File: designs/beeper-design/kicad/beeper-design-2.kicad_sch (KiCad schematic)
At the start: 26 parts, among them U14 EVPBB4A9B000, U15 EVPBB4A9B000, U16 EVPBB4A9B000, U4 DA7212-01UM2, U9 LSM6DSOXTR

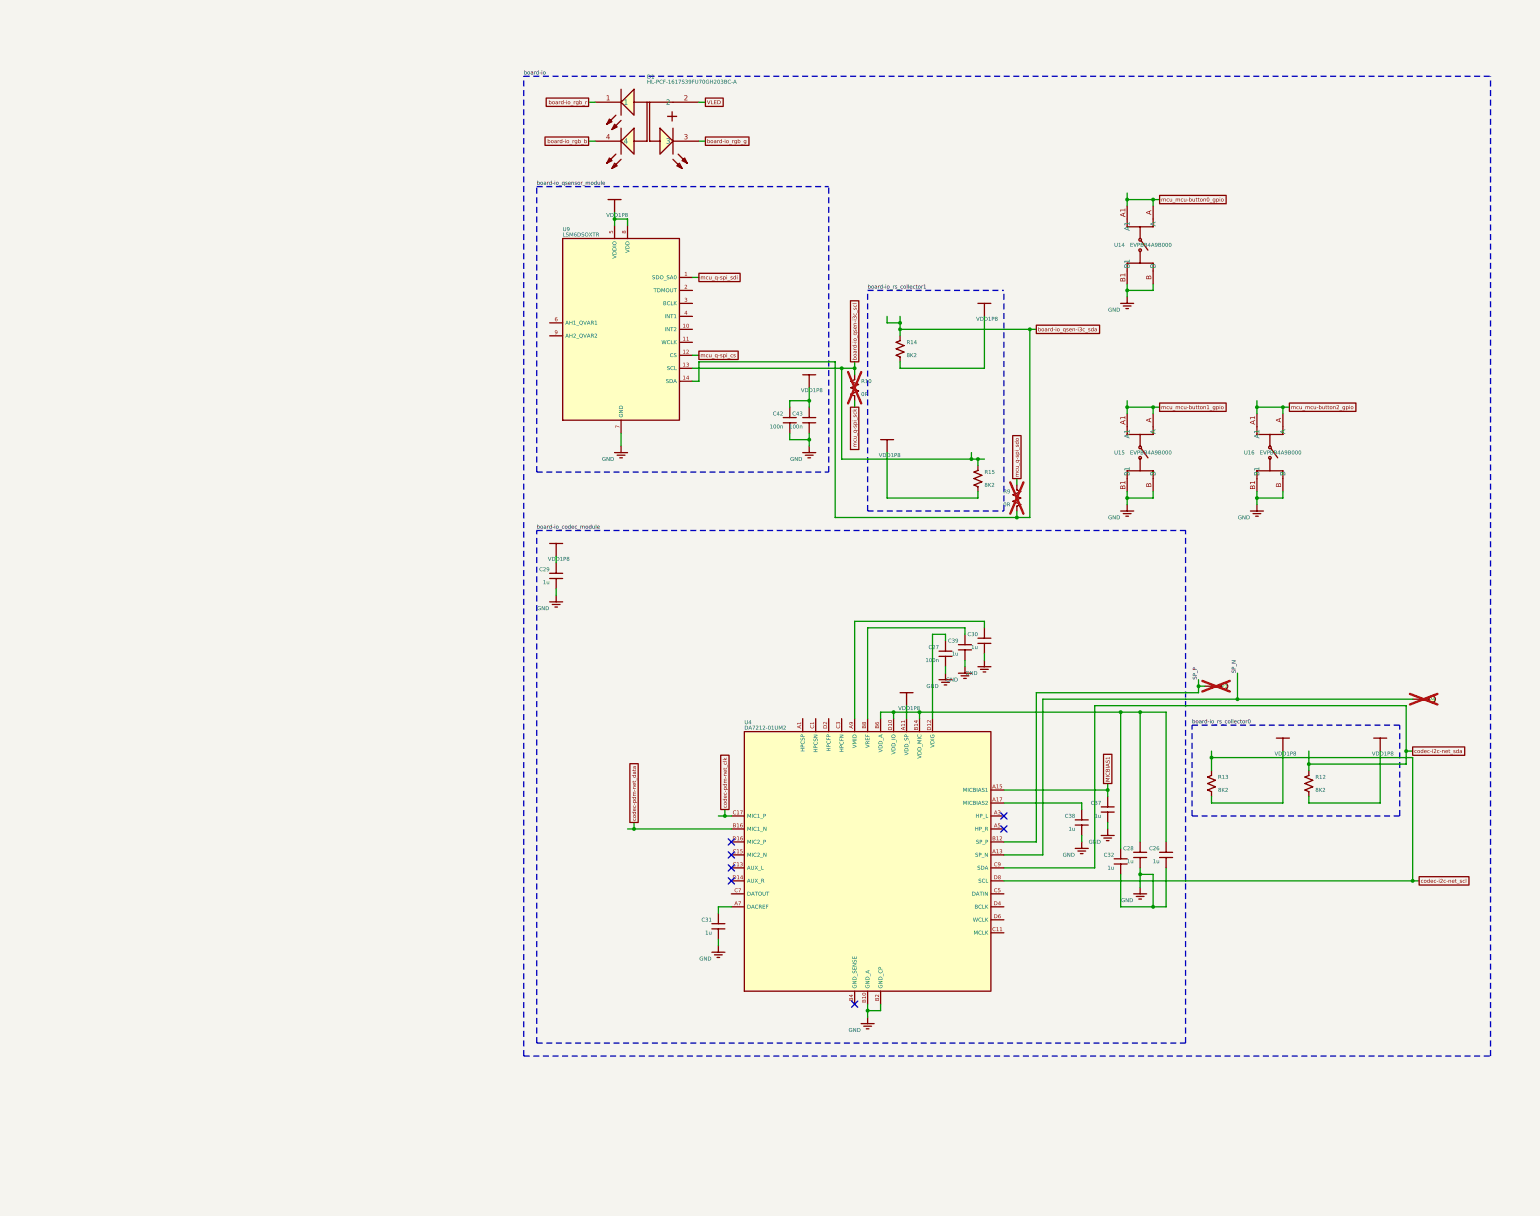
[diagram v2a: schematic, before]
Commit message: fixing drc errors
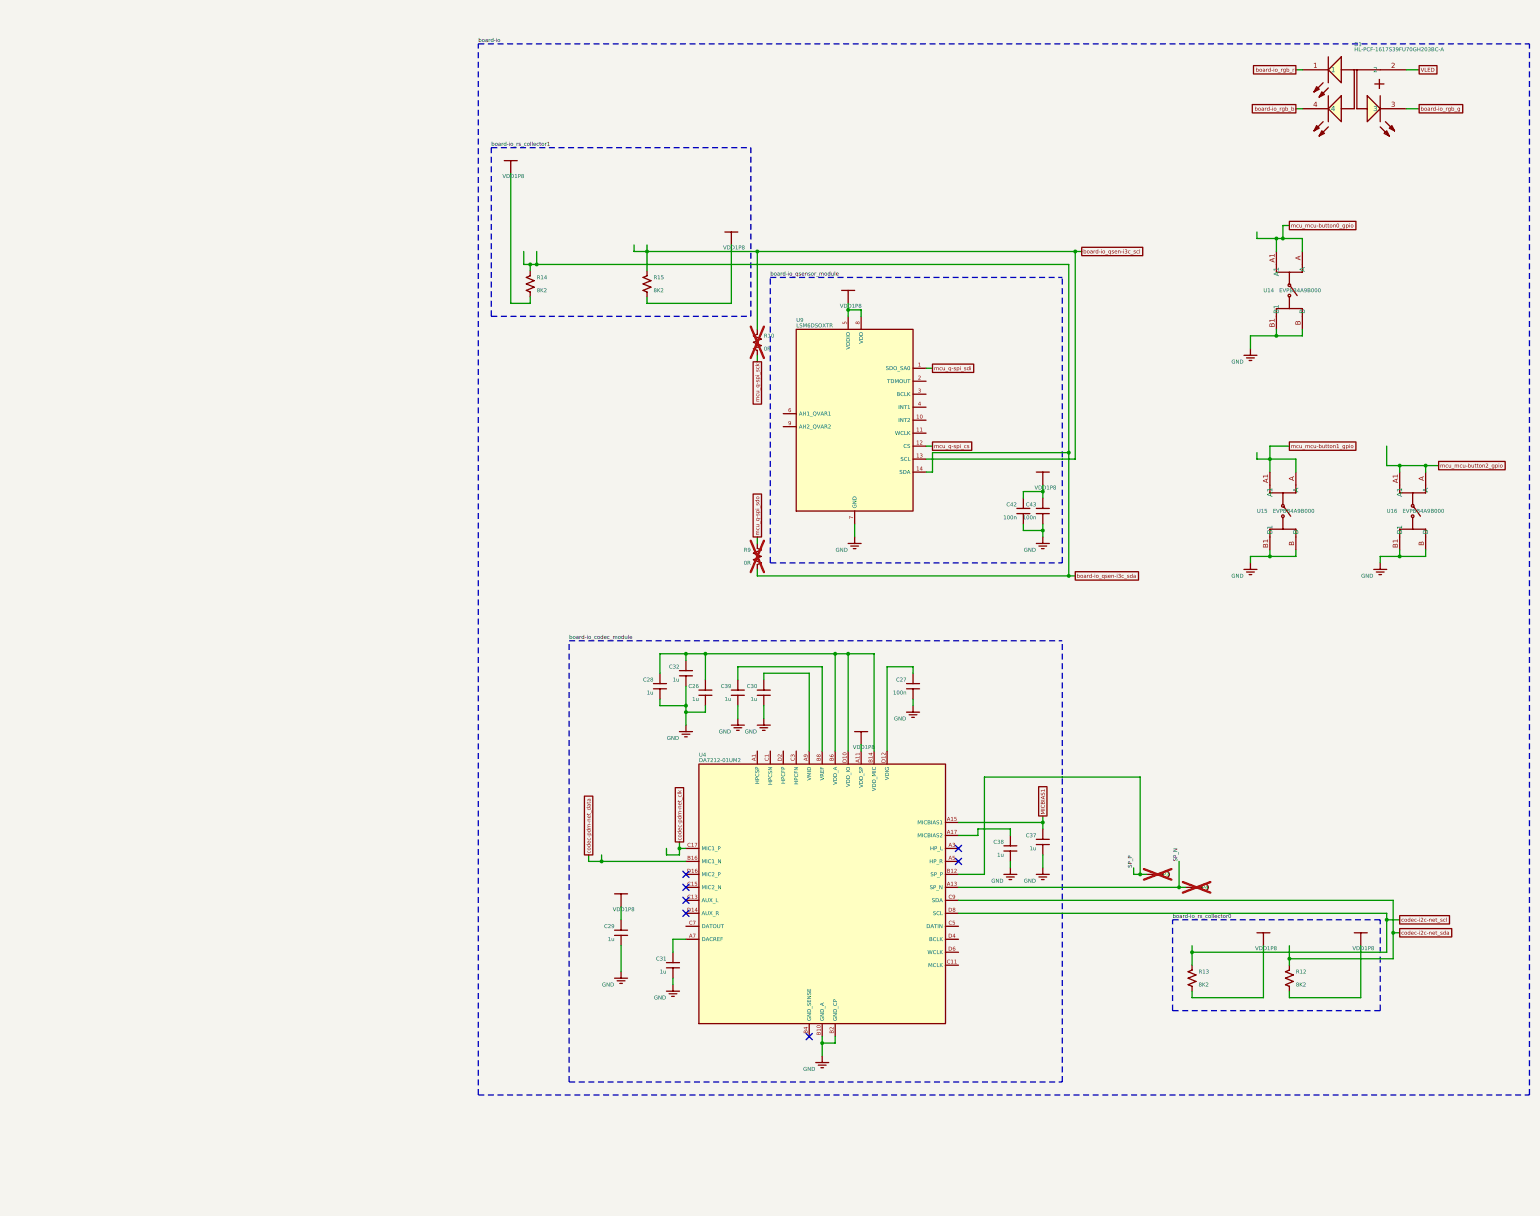
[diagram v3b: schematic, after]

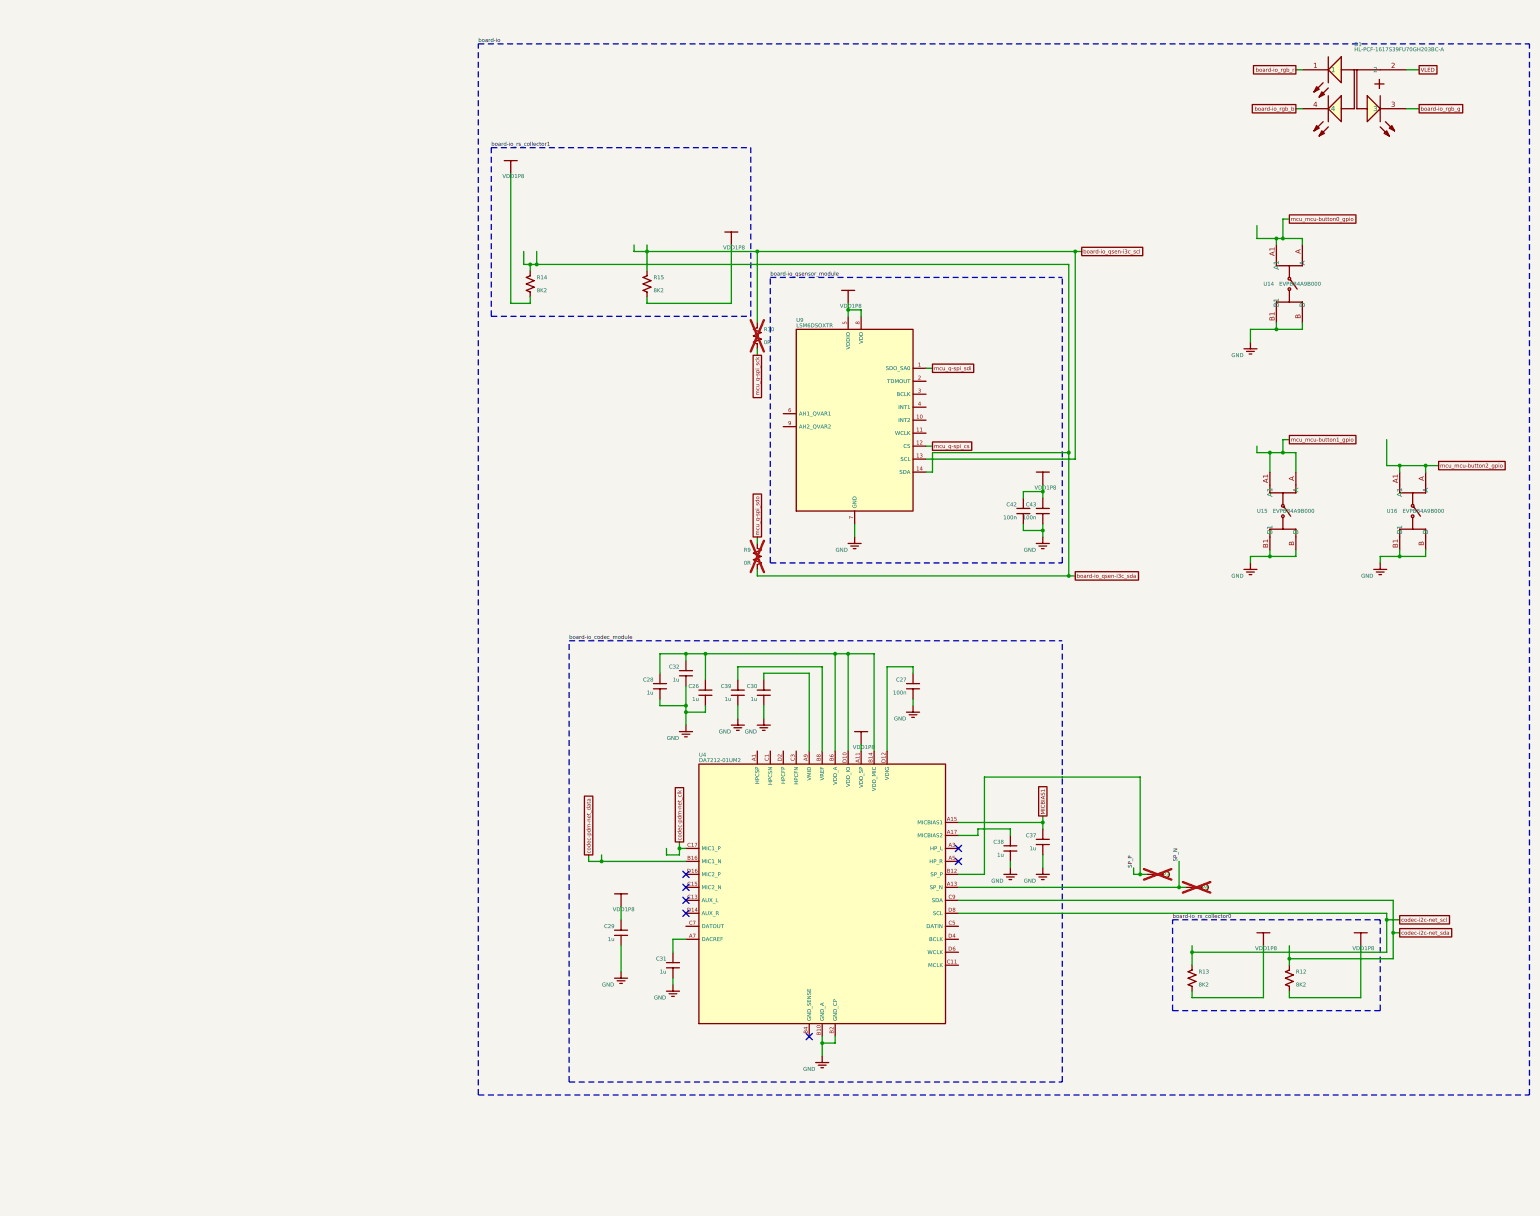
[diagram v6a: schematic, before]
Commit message: made ocdb a submodule
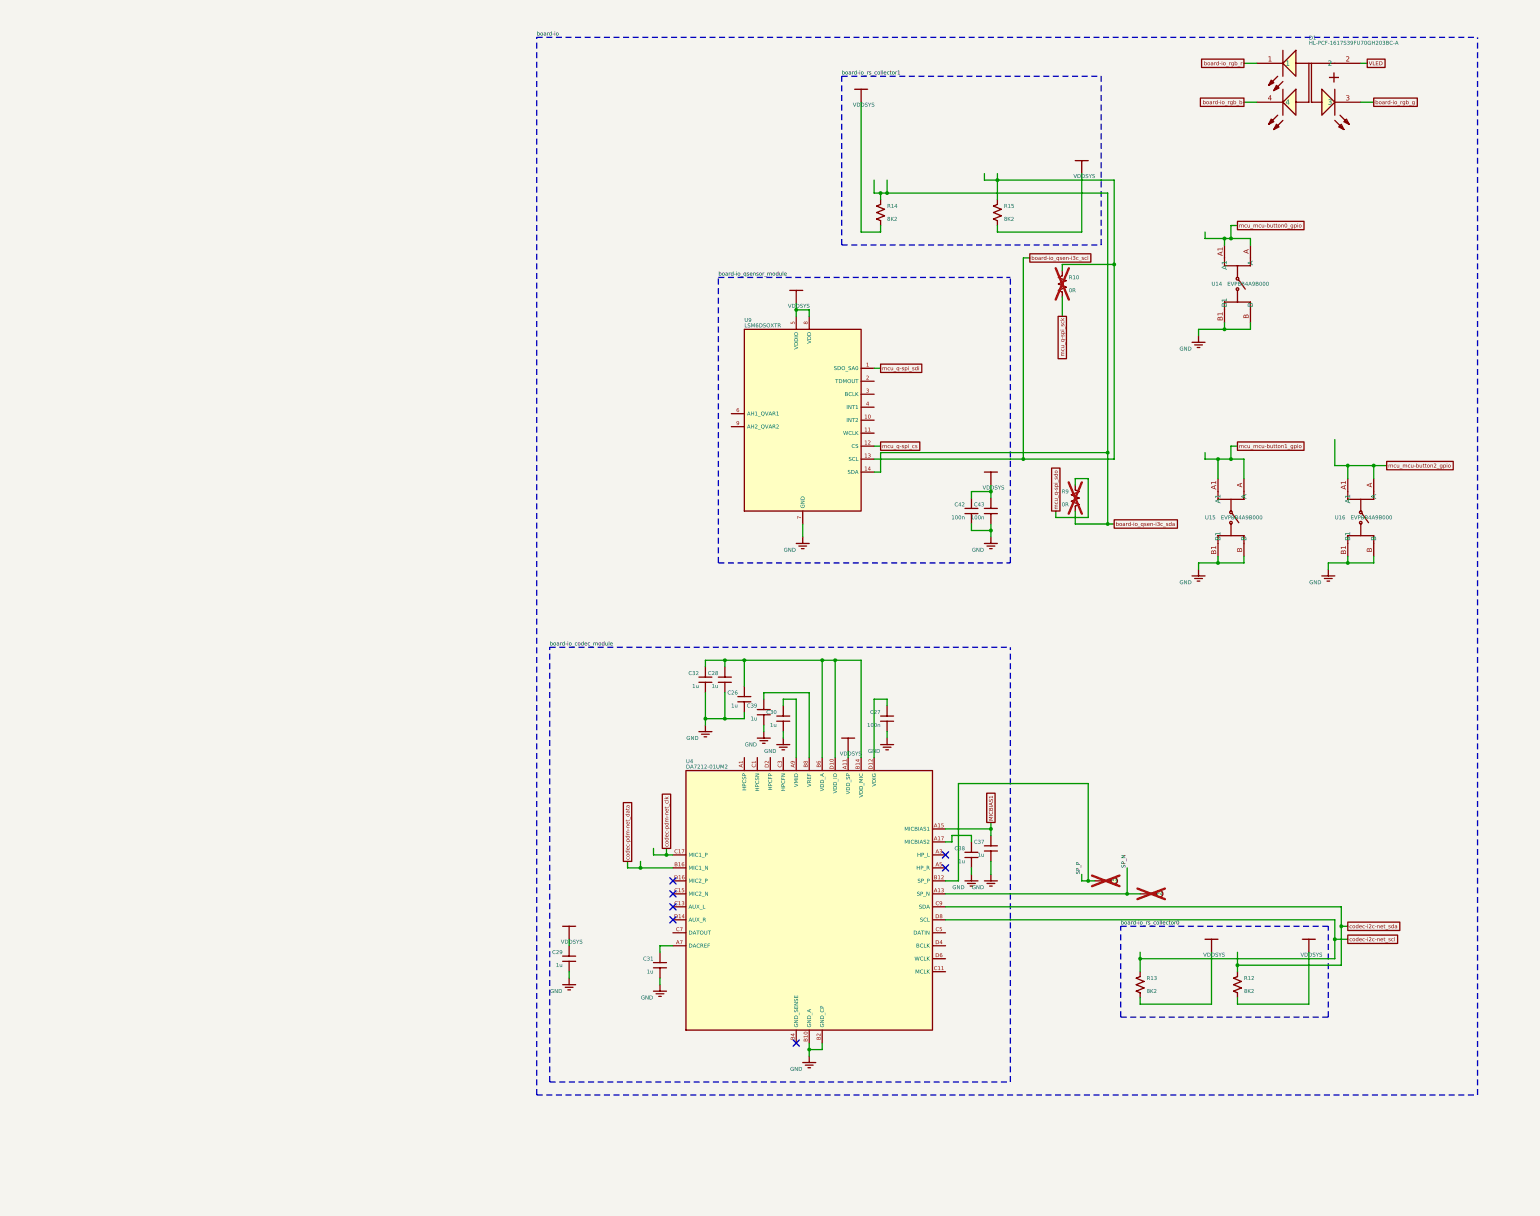
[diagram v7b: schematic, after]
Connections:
- net VDD1P8 renamed VDDSYS

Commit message: kicad exported data
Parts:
- removed C26: 1u, beeper-design:Pkg0201_27, symbol C76935_8
- removed C27: 100n, beeper-design:Pkg0201_38, symbol my_capacitor_13
- removed C28: 1u, beeper-design:Pkg0201_5, symbol C76935_1
- removed C29: 1u, beeper-design:Pkg0201_15, symbol C76935_5
- removed C30: 1u, beeper-design:Pkg0201_3, symbol C76935
- removed C31: 1u, beeper-design:Pkg0201_13, symbol C76935_4
- removed C32: 1u, beeper-design:Pkg0201_23, symbol C76935_6
- removed C37: 1u, beeper-design:Pkg0201_26, symbol C76935_7
- removed C38: 1u, beeper-design:Pkg0201_37, symbol C76935_10
- removed C39: 1u, beeper-design:Pkg0201_35, symbol C76935_9
- removed C42: 100n, beeper-design:Pkg0201_29, symbol my_capacitor_8
- removed C43: 100n, beeper-design:Pkg0201_39, symbol my_capacitor_14
- removed R10: 0R, beeper-design:Pkg0201_28, symbol my_resistor_8
- removed R12, R13: 8K2, beeper-design:Pkg0201_17, symbol my_resistor_4
- removed R14, R15: 8K2, beeper-design:Pkg0201_1, symbol my_resistor
- removed R9: 0R, beeper-design:Pkg0201_19, symbol my_resistor_5
- removed U4: DA7212-01UM2, beeper-design:LP_3, symbol component_1
- added C26: 2.2u, beeper-design:Pkg0201_19, symbol C335106_10
- added C27: 2.2u, beeper-design:Pkg0201_33, symbol C335106_21
- added C28: 2.2u, beeper-design:Pkg0201_46, symbol C335106_28
- added C29: 2.2u, beeper-design:Pkg0201_3, symbol C335106
- added C30: 2.2u, beeper-design:Pkg0201_43, symbol C335106_27
- added C31: 2.2u, beeper-design:Pkg0201, symbol C335106_36
- added C32: 2.2u, beeper-design:Pkg0201_12, symbol C335106_6
- added C37: 2.2u, beeper-design:Pkg0201_17, symbol C335106_8
- added C38: 2.2u, beeper-design:Pkg0201_31, symbol C335106_20
- added C39: 2.2u, beeper-design:Pkg0201_28, symbol C335106_18
- added C42: 2.2u, beeper-design:Pkg0201_21, symbol C335106_11
- added C43: 2.2u, beeper-design:Pkg0201_34, symbol C335106_22
- added R10: 0R, beeper-design:Pkg0201_20, symbol my_resistor_5
- added R12, R13: 8K2, beeper-design:Pkg0201_5, symbol my_resistor_1
- added R14, R15: 8K2, beeper-design:Pkg0201_42, symbol my_resistor_10
- added R9: 0R, beeper-design:Pkg0201_7, symbol my_resistor_2
- added U4: DA7212-01UM2, beeper-design:LP_3, symbol component
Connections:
- net GND: now also C26.1, C27.1, C28.1, C29.1, C30.1, C31.1, C32.1, C37.1, C38.1, C39.1, C42.1, C43.1, U4.B10 (GND_A), U4.B2 (GND_CP)
- net MICBIAS1: now also C37.2, U4.A15 (MICBIAS1)
- net SP_N: now also U4.A13 (SP_N)
- net SP_P: now also U4.B12 (SP_P)
- net board-io_qsen-i3c_scl: now also R10.1, R15.1
- net codec-i2c-net_scl: now also R13.1, U4.D8 (SCL)
- net codec-i2c-net_sda: now also R12.1, U4.C9 (SDA)
- net codec-pdm-net_clk: now also U4.C17 (MIC1_P)
- net codec-pdm-net_data: now also U4.B16 (MIC1_N)
- net mcu_q-spi_sck: now also R10.2
- net mcu_q-spi_sdo: now also R9.2
- net VDDSYS renamed VDD1P8
- net VDD1P8: now also C29.2, C42.2, C43.2, R12.2, R13.2, R14.2, R15.2, U4.A11 (VDD_SP)
- net board-io_qsen-i3c_sda renamed mcu_q-i3c_sda
- net mcu_q-i3c_sda: now also R14.1, R9.1
- new net: C39.2, U4.B8 (VREF)
- new net: C26.2, C28.2, C32.2, U4.B14 (VDD_MIC), U4.B6 (VDD_A), U4.D10 (VDD_IO)
- new net: C27.2, U4.D12 (VDIG)
- new net: C38.2, U4.A17 (MICBIAS2)
- new net: C31.2, U4.A7 (DACREF)
- new net: C30.2, U4.A9 (VMID)
